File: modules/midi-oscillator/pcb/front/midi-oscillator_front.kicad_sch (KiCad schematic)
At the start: 45 parts, among them SW1 PEC11R-4220K-S0024

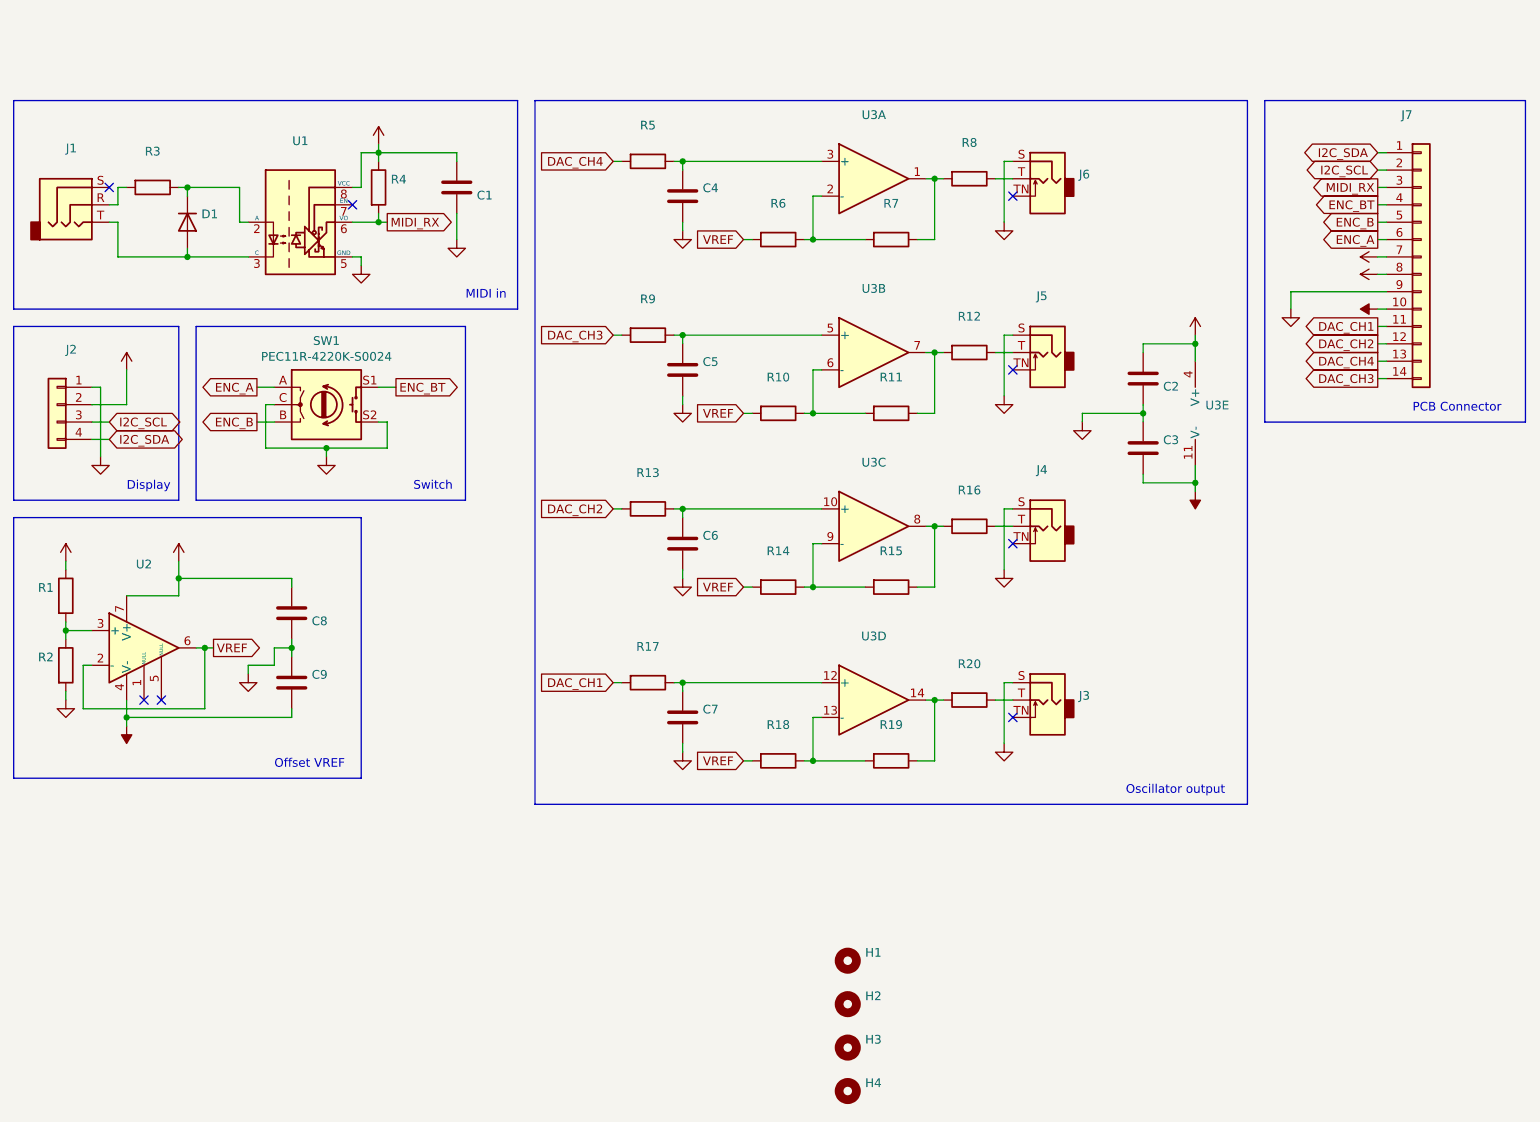
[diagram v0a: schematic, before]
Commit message: modules: midi-oscillator: front: new revision 1.1
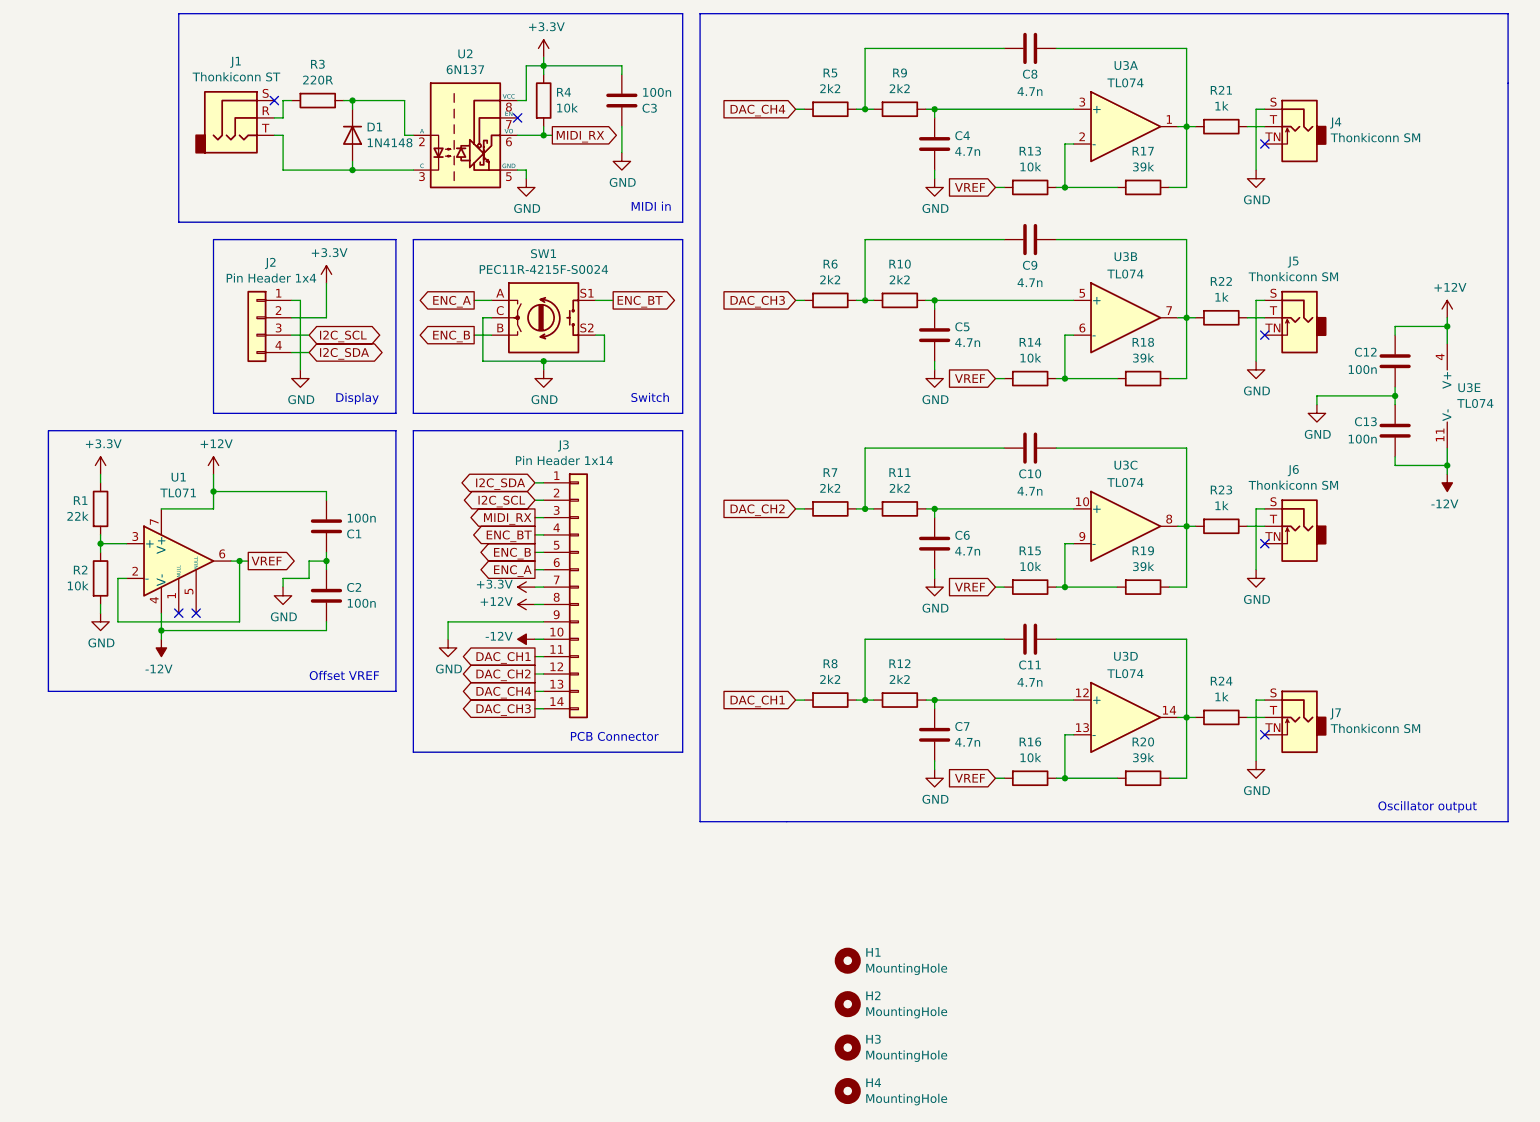
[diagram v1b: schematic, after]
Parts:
- removed R13, R17: (no value), symbol Device:R
- added C10, C11, C8, C9: 4.7n, Capacitor_THT:C_Rect_L7.0mm_W2.5mm_P5.00mm, symbol Device:C
- added R12, R6, R7, R8: 2k2, Resistor_THT:R_Axial_DIN0207_L6.3mm_D2.5mm_P10.16mm_Horizontal, symbol Device:R
- added R16: 10k, Resistor_THT:R_Axial_DIN0207_L6.3mm_D2.5mm_P10.16mm_Horizontal, symbol Device:R
- added R20: 39k, Resistor_THT:R_Axial_DIN0207_L6.3mm_D2.5mm_P10.16mm_Horizontal, symbol Device:R
- C1: renamed from C8; value (none) -> 100n; footprint (none) -> Capacitor_THT:C_Disc_D4.3mm_W1.9mm_P5.00mm
- C12: renamed from C2; value (none) -> 100n; footprint (none) -> Capacitor_THT:C_Disc_D4.3mm_W1.9mm_P5.00mm
- C13: renamed from C3; value (none) -> 100n; footprint (none) -> Capacitor_THT:C_Disc_D4.3mm_W1.9mm_P5.00mm
- C2: renamed from C9; value (none) -> 100n; footprint (none) -> Capacitor_THT:C_Disc_D4.3mm_W1.9mm_P5.00mm
- C3: renamed from C1; value (none) -> 100n; footprint (none) -> Capacitor_THT:C_Disc_D4.3mm_W1.9mm_P5.00mm
- C4, C5, C6, C7: value (none) -> 4.7n; footprint (none) -> Capacitor_THT:C_Rect_L7.0mm_W2.5mm_P5.00mm
- D1: value (none) -> 1N4148; footprint (none) -> Diode_THT:D_DO-35_SOD27_P7.62mm_Horizontal
- H1, H2, H3, H4: value (none) -> MountingHole; footprint (none) -> MountingHole:MountingHole_2.2mm_M2
- J1: value (none) -> Thonkiconn ST; footprint (none) -> eurorack:Jack_3.5mm_QingPu_WQP-PJ366ST_Vertical
- J2: value (none) -> Pin Header 1x4; footprint (none) -> Connector_PinSocket_2.54mm:PinSocket_1x04_P2.54mm_Vertical
- J3: renamed from J7; value (none) -> Pin Header 1x14; footprint (none) -> Connector_PinHeader_2.54mm:PinHeader_1x14_P2.54mm_Vertical
- J4: renamed from J6; value (none) -> Thonkiconn SM; footprint (none) -> eurorack:Jack_3.5mm_QingPu_WQP-PJ398SM_Vertical
- J5: value (none) -> Thonkiconn SM; footprint (none) -> eurorack:Jack_3.5mm_QingPu_WQP-PJ398SM_Vertical
- J6: renamed from J4; value (none) -> Thonkiconn SM; footprint (none) -> eurorack:Jack_3.5mm_QingPu_WQP-PJ398SM_Vertical
- J7: renamed from J3; value (none) -> Thonkiconn SM; footprint (none) -> eurorack:Jack_3.5mm_QingPu_WQP-PJ398SM_Vertical
- R1: value (none) -> 22k; footprint (none) -> Resistor_THT:R_Axial_DIN0207_L6.3mm_D2.5mm_P10.16mm_Horizontal
- R10, R11, R5, R9: value (none) -> 2k2; footprint (none) -> Resistor_THT:R_Axial_DIN0207_L6.3mm_D2.5mm_P10.16mm_Horizontal
- R13: renamed from R6; value (none) -> 10k; footprint (none) -> Resistor_THT:R_Axial_DIN0207_L6.3mm_D2.5mm_P10.16mm_Horizontal
- R14, R15, R2, R4: value (none) -> 10k; footprint (none) -> Resistor_THT:R_Axial_DIN0207_L6.3mm_D2.5mm_P10.16mm_Horizontal
- R17: renamed from R7; value (none) -> 39k; footprint (none) -> Resistor_THT:R_Axial_DIN0207_L6.3mm_D2.5mm_P10.16mm_Horizontal
- R18, R19: value (none) -> 39k; footprint (none) -> Resistor_THT:R_Axial_DIN0207_L6.3mm_D2.5mm_P10.16mm_Horizontal
- R21: renamed from R8; value (none) -> 1k; footprint (none) -> Resistor_THT:R_Axial_DIN0207_L6.3mm_D2.5mm_P10.16mm_Horizontal
- R22: renamed from R12; value (none) -> 1k; footprint (none) -> Resistor_THT:R_Axial_DIN0207_L6.3mm_D2.5mm_P10.16mm_Horizontal
- R23: renamed from R16; value (none) -> 1k; footprint (none) -> Resistor_THT:R_Axial_DIN0207_L6.3mm_D2.5mm_P10.16mm_Horizontal
- R24: renamed from R20; value (none) -> 1k; footprint (none) -> Resistor_THT:R_Axial_DIN0207_L6.3mm_D2.5mm_P10.16mm_Horizontal
- R3: value (none) -> 220R; footprint (none) -> Resistor_THT:R_Axial_DIN0207_L6.3mm_D2.5mm_P10.16mm_Horizontal
- SW1: value PEC11R-4220K-S0024 -> PEC11R-4215F-S0024
- U1: renamed from U2; value (none) -> TL071; footprint (none) -> Package_DIP:DIP-8_W7.62mm
- U2: renamed from U1; value (none) -> 6N137; footprint (none) -> Package_DIP:DIP-8_W7.62mm
- U3: value (none) -> TL074; footprint (none) -> Package_DIP:DIP-14_W7.62mm
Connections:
- net DAC_CH1: now also R8.2
- net DAC_CH2: now also R7.2
- net DAC_CH3: now also R6.2; no longer R9.2
- net VREF: now also R15.2, R16.2; no longer R10.2, R18.2
- net at R22.2, U3.7: now also R18.1, C9.2; no longer R11.1
- net at C5.1, U3.5 (+): now also R10.1; no longer R9.1
- net at R23.2, U3.8: now also R19.1, C10.2; no longer R15.1
- net at C6.1, U3.10 (+): now also R11.1
- net at R24.2, U3.14: now also C11.2, R20.1; no longer R19.1
- net at C7.1, U3.12 (+): now also R12.1
- net at R17.1, R21.2, U3.1: now also C8.2
- net at C4.1, U3.3 (+): now also R9.1; no longer R5.1
- net +3V3 renamed +3.3V
- new net: C8.1, R5.1, R9.2
- new net: C9.1, R10.2, R6.1
- new net: R15.1, R19.2, U3.9 (-)
- new net: R14.1, R18.2, U3.6 (-)
- new net: C11.1, R12.2, R8.1
- new net: R16.1, R20.2, U3.13 (-)
- new net: C10.1, R11.2, R7.1
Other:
- title: midi-controller front -> midi-oscillator front
- moved on the sheet: C1, C12, C13, C2, C3, C4, D1, J1, J2, J3, J4, J5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
